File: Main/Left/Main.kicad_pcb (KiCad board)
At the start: 2 copper layers, 140.2 x 97.8 mm, 44 parts, among them SW1 RotaryEncoder_Switch_MP, SW2 Switch, U1 Arduino_Pro_Micro, U2 TRRS

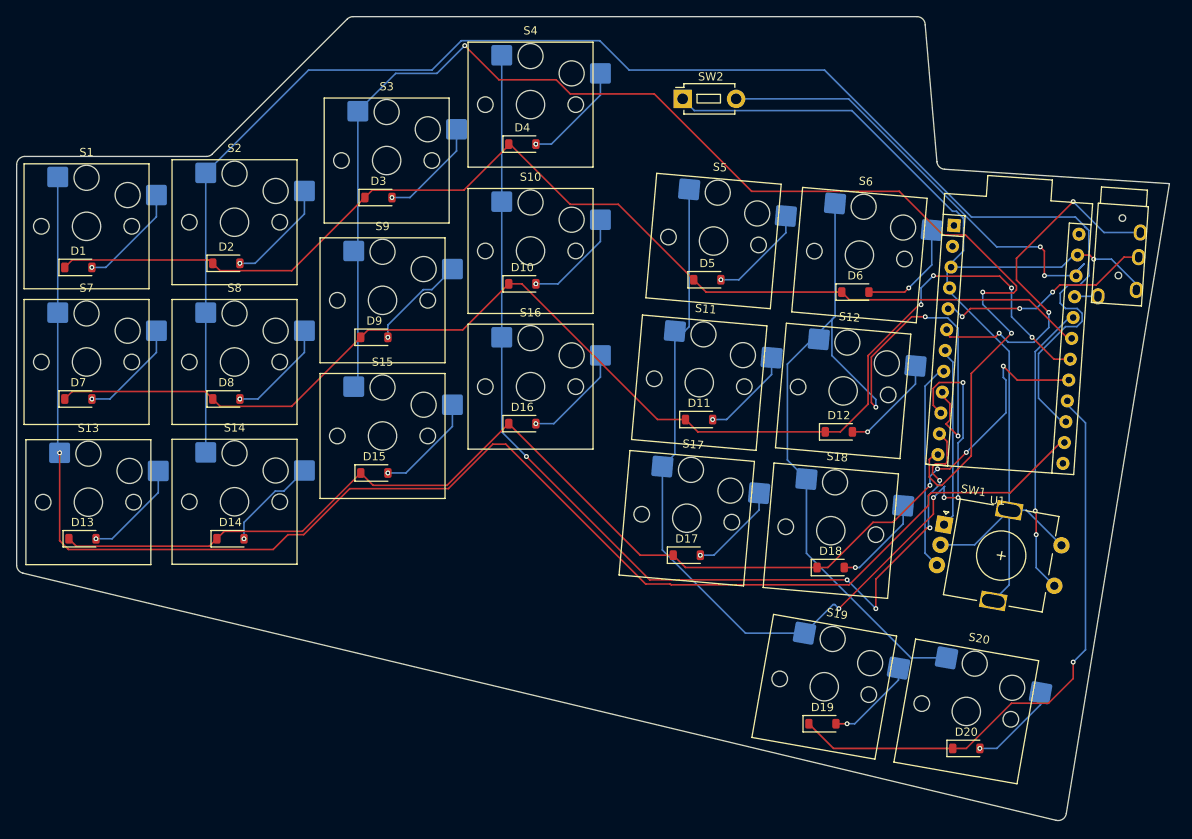
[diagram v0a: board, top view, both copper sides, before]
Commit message: changed from I2C communication between the halves to serial because it's easier with QMK
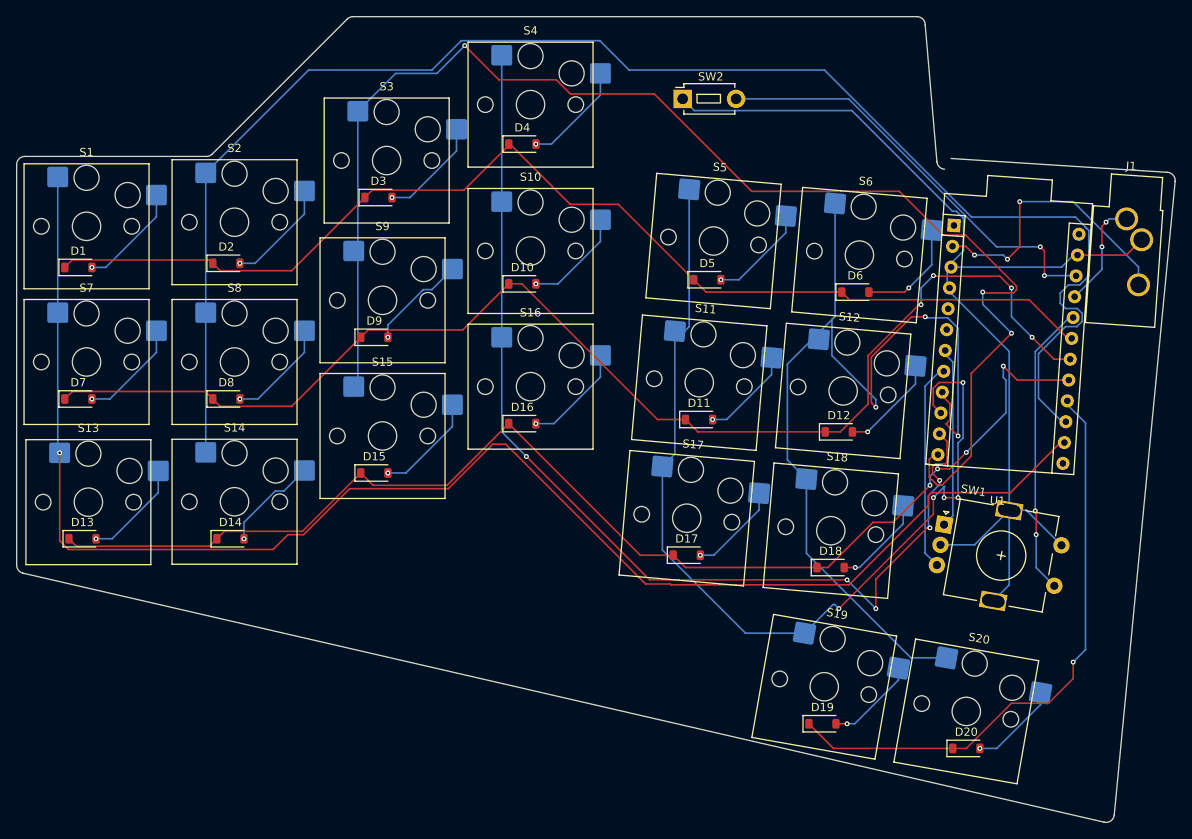
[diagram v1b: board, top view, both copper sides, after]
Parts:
- removed U2: TRRS, ScottoKeebs_Components:TRRS_PJ-320A
- added J1: AudioJack3, Connector_Audio:Jack_3.5mm_CUI_SJ1-3533NG_Horizontal_CircularHoles, F.Cu at (281.0, 74.6)
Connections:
- U1 pad 2: unconnected-(U1-RX1/PD2-Pad2) -> Serial
- U1 pad 5: SDA -> unconnected-(U1-2/PD1-Pad5)
- U1 pad 6: SCL -> unconnected-(U1-3/PD0-Pad6)
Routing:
- net SCL: track 44.2 -> 0.00 mm, vias 3 -> 0
- net Serial: track 0.00 -> 35.5 mm, vias 0 -> 3
- net SDA: track 27.0 -> 0.00 mm, vias 3 -> 0
- net VCC: track 2.85 -> 13.4 mm, vias 0 -> 2
- net RST: track 55.6 -> 51.6 mm
- net GND: track 135.6 -> 134.4 mm, vias 1 -> 0
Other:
- board size 140.2 x 97.8 mm -> 140.9 x 98 mm
